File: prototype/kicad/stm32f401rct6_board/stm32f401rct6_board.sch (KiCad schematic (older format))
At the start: 1 part

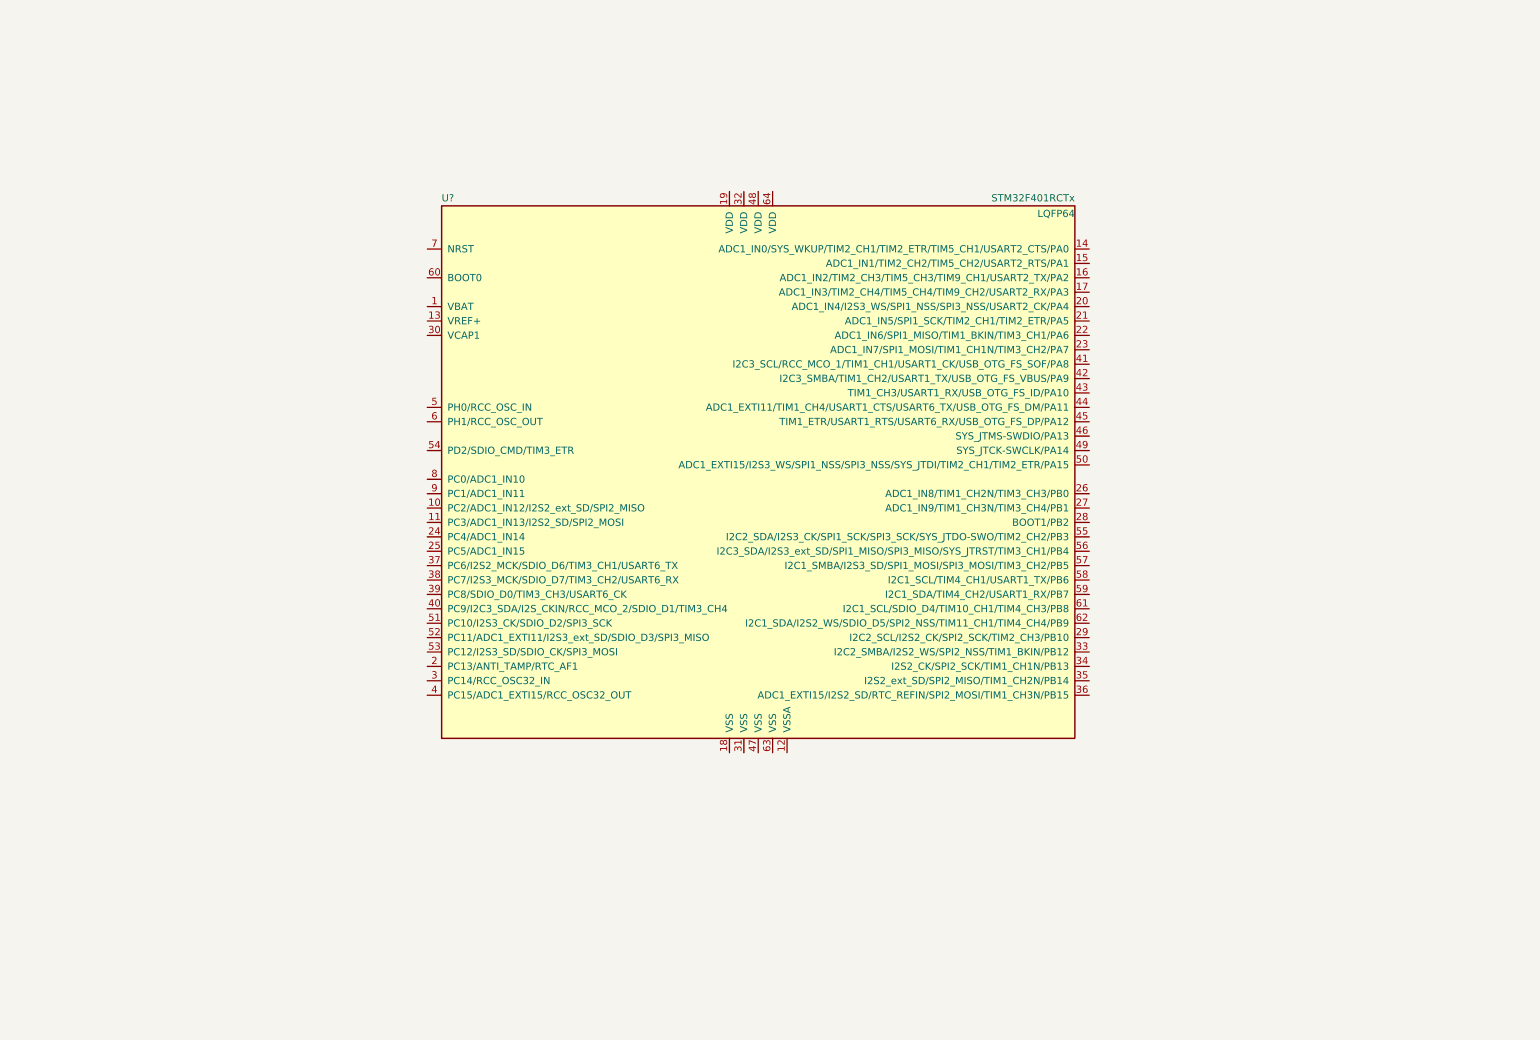
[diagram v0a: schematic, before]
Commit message: USART, boot switches, power supplies are implemented.
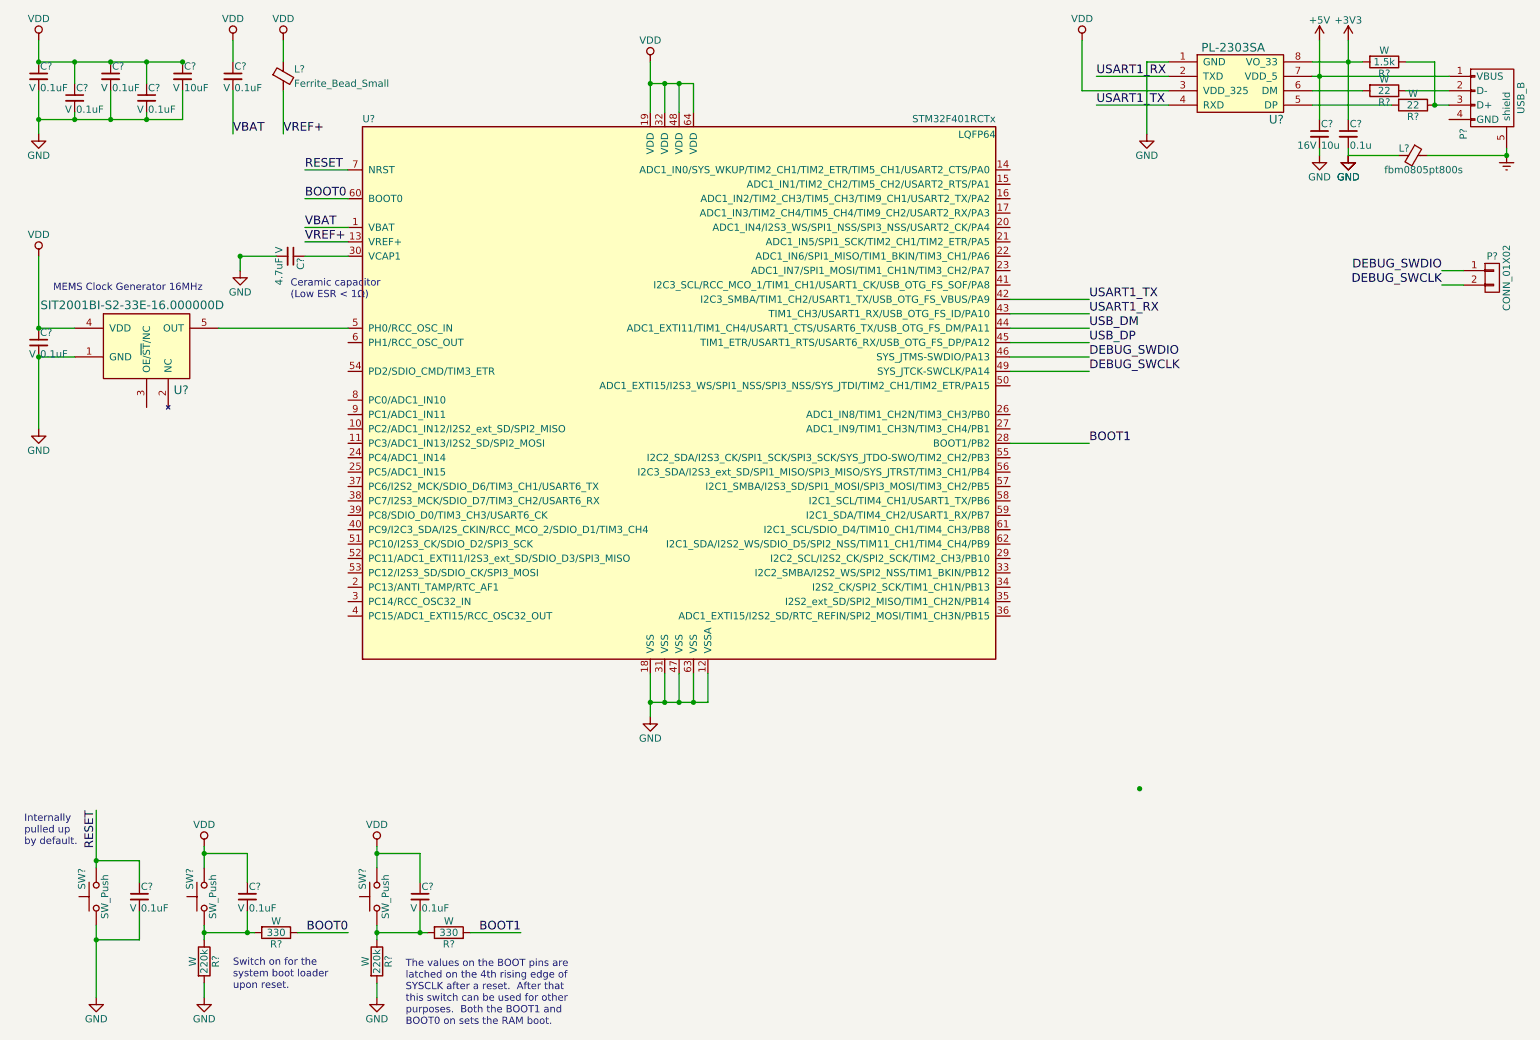
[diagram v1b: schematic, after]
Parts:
- added C? (x9): 0.1uF, symbol C_Small
- added C?: 10uF, symbol C_Small
- added C?: 4.7uF, symbol C_Small
- added C?: 10u, symbol C_Small
- added C?: 0.1u, symbol C_Small
- added L?: Ferrite_Bead_Small, symbol Ferrite_Bead_Small
- added L?: fbm0805pt800s, symbol Ferrite_Bead_Small
- added P?: CONN_01X02, symbol CONN_01X02
- added P?: USB_B, symbol USB_B
- added R? (x2): 220k, symbol R
- added R? (x2): 330, symbol R
- added R? (x2): 22, symbol R
- added R?: 1.5k, symbol R
- added SW? (x3): SW_Push, symbol SW_Push
- added U?: SIT2001BI-S2-33E-16.000000D, symbol SiT2001B
- added U?: PL-2303SA, symbol PL-2303SA
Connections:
- net VBAT: now reaches U?.1 (VBAT)
- net VBAT: now also C?.2
- net GND: now reaches U?.12 (VSSA)
- net GND: now also U?.18 (VSS), U?.31 (VSS), U?.47 (VSS), U?.63 (VSS), C?.2, C?.2, C?.2, C?.2, C?.2, C?.2, C?.2, C?.2, C?.2, C?.2, L?.2, R?.2, R?.2, SW?.1, U?.1 (GND), U?.1 (GND)
- net VREF+: now reaches U?.13 (VREF+)
- net VREF+: now also L?.2
- net VDD: now reaches U?.19 (VDD)
- net VDD: now also U?.32 (VDD), U?.48 (VDD), U?.64 (VDD), C?.1, C?.1, C?.1, C?.1, C?.1, C?.1, C?.1, C?.1, C?.1, L?.1, SW?.2, SW?.2, U?.3 (VDD_325), U?.4 (VDD)
- net BOOT1: now reaches U?.28 (BOOT1/PB2)
- net BOOT1: now also R?.1
- net at U?.30 (VCAP1): now also C?.1
- net USART1_TX: now reaches U?.42 (I2C3_SMBA/TIM1_CH2/USART1_TX/USB_OTG_FS_VBUS/PA9)
- net USART1_TX: now also U?.4 (RXD)
- net USART1_RX: now reaches U?.43 (TIM1_CH3/USART1_RX/USB_OTG_FS_ID/PA10)
- net USART1_RX: now also U?.2 (TXD)
- net USB_DM: now reaches U?.44 (ADC1_EXTI11/TIM1_CH4/USART1_CTS/USART6_TX/USB_OTG_FS_DM/PA11)
- net USB_DP: now reaches U?.45 (TIM1_ETR/USART1_RTS/USART6_RX/USB_OTG_FS_DP/PA12)
- net DEBUG_SWDIO: now reaches U?.46 (SYS_JTMS-SWDIO/PA13)
- net DEBUG_SWDIO: now also P?.1 (P1)
- net DEBUG_SWCLK: now reaches U?.49 (SYS_JTCK-SWCLK/PA14)
- net DEBUG_SWCLK: now also P?.2 (P2)
- net at U?.5 (PH0/RCC_OSC_IN): now also U?.5 (OUT)
- net BOOT0: now reaches U?.60 (BOOT0)
- net BOOT0: now also R?.1
- net RESET: now reaches U?.7 (NRST)
- net RESET: now also C?.1, SW?.2
- new net: C?.2, R?.1, R?.2, SW?.1 (x2)
- new net: R?.2, U?.5 (DP)
- new net: R?.2, U?.6 (DM)
- new net: P?.2 (D-), R?.1
- new net: P?.3 (D+), R?.1, R?.1
- new net +3V3: C?.1, R?.2, U?.8 (VO_33)
- new net +5V: C?.1, P?.1 (VBUS), U?.7 (VDD_5)
- new net Earth: L?.1, P?.5 (shield)
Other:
- note added: "Ceramic capacitor \n(Low ESR < 1Ω)"
- note added: "Internally\npulled up\nby default."
- note added: "MEMS Clock Generator 16MHz"
- note added: "Switch on for the\nsystem boot loader\nupon reset."
- note added: "The values on the BOOT pins are\nlatched on the 4th rising edge of\nSYSCLK after a reset. After that\nthis switch can be used for other\npurposes. Both the BOOT1 and\nBOOT0 on sets the RAM boot.\n"
- moved on the sheet: U?

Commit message: added some parts
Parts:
- added P?: USB_OTG, symbol USB_OTG
- added U?: STMPS2141STR, symbol STMPS2141STR
- added U?: EMIF02-USB03F2, symbol EMIF02-USB03F2
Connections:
- net GND: now also P?.4 (GND)
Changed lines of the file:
@@
 USB_DP
 $Comp
-L VDD #PWR?
+L VDD #PWR01
 U 1 1 592E7F1B
 P 750 2350
-F 0 "#PWR?" H 750 2200 50  0001 C CNN
+F 0 "#PWR01" H 750 2200 50  0001 C CNN
 F 1 "VDD" H 750 2500 50  0000 C CNN
 F 2 "" H 750 2350 50  0000 C CNN
@@
 $EndComp
 $Comp
-L GND #PWR?
+L GND #PWR02
 U 1 1 592E7F48
 P 750 3550
-F 0 "#PWR?" H 750 3300 50  0001 C CNN
+F 0 "#PWR02" H 750 3300 50  0001 C CNN
 F 1 "GND" H 750 3400 50  0000 C CNN
 F 2 "" H 750 3550 50  0000 C CNN
@@
 $EndComp
 $Comp
-L VDD #PWR?
+L VDD #PWR03
 U 1 1 592E82FC
 P 5000 1000
-F 0 "#PWR?" H 5000 850 50  0001 C CNN
+F 0 "#PWR03" H 5000 850 50  0001 C CNN
 F 1 "VDD" H 5000 1150 50  0000 C CNN
 F 2 "" H 5000 1000 50  0000 C CNN
@@
 $EndComp
 $Comp
-L GND #PWR?
+L GND #PWR04
 U 1 1 592E8A90
 P 750 1500
-F 0 "#PWR?" H 750 1250 50  0001 C CNN
+F 0 "#PWR04" H 750 1250 50  0001 C CNN
 F 1 "GND" H 750 1350 50  0000 C CNN
 F 2 "" H 750 1500 50  0000 C CNN
@@
 $EndComp
 $Comp
-L VDD #PWR?
+L VDD #PWR05
 U 1 1 592E8AD2
 P 750 850
-F 0 "#PWR?" H 750 700 50  0001 C CNN
+F 0 "#PWR05" H 750 700 50  0001 C CNN
 F 1 "VDD" H 750 1000 50  0000 C CNN
 F 2 "" H 750 850 50  0000 C CNN
@@
 $EndComp
 $Comp
-L VDD #PWR?
+L VDD #PWR06
 U 1 1 592E9827
 P 2100 850
-F 0 "#PWR?" H 2100 700 50  0001 C CNN
+F 0 "#PWR06" H 2100 700 50  0001 C CNN
 F 1 "VDD" H 2100 1000 50  0000 C CNN
 F 2 "" H 2100 850 50  0000 C CNN
@@
 VBAT
 $Comp
-L VDD #PWR?
+L VDD #PWR07
 U 1 1 592E99F2
 P 2450 850
-F 0 "#PWR?" H 2450 700 50  0001 C CNN
+F 0 "#PWR07" H 2450 700 50  0001 C CNN
 F 1 "VDD" H 2450 1000 50  0000 C CNN
 F 2 "" H 2450 850 50  0000 C CNN
@@
 $EndComp
 $Comp
-L GND #PWR?
+L GND #PWR08
 U 1 1 592EC658
 P 2150 2450
-F 0 "#PWR?" H 2150 2200 50  0001 C CNN
+F 0 "#PWR08" H 2150 2200 50  0001 C CNN
 F 1 "GND" H 2150 2300 50  0000 C CNN
 F 2 "" H 2150 2450 50  0000 C CNN
@@
 	7500 2950 8050 2950
 Wire Wire Line
-	5000 1000 5000 1150
-Wire Wire Line
-	5000 1150 5000 1350
+	5000 1000 5000 1350
 Wire Wire Line
 	5100 1350 5100 1150
@@
 	5300 1150 5300 1350
 Wire Wire Line
-	5000 1150 5100 1150
-Wire Wire Line
-	5100 1150 5200 1150
-Wire Wire Line
-	5200 1150 5300 1150
+	5000 1150 5300 1150
 Connection ~ 5000 1150
 Connection ~ 5200 1150
@@
 	750  850  750  1000
 Wire Wire Line
-	750  1000 1000 1000
-Wire Wire Line
-	1000 1000 1250 1000
-Wire Wire Line
-	1250 1000 1500 1000
-Wire Wire Line
-	1500 1000 1750 1000
-Wire Wire Line
-	750  1200 750  1400
-Wire Wire Line
-	750  1400 750  1500
+	750  1000 1750 1000
+Wire Wire Line
+	750  1200 750  1500
 Wire Wire Line
 	1000 1000 1000 1150
@@
 	1750 1400 1750 1200
 Wire Wire Line
-	750  1400 1000 1400
-Wire Wire Line
-	1000 1400 1250 1400
-Wire Wire Line
-	1250 1400 1500 1400
-Wire Wire Line
-	1500 1400 1750 1400
+	750  1400 1750 1400
 Connection ~ 1500 1400
 Connection ~ 1250 1400
@@
 	2150 2350 2150 2450
 Wire Wire Line
-	5000 5250 5000 5450
-Wire Wire Line
-	5000 5450 5000 5550
+	5000 5250 5000 5550
 Wire Wire Line
 	5100 5250 5100 5450
@@
 	5400 5450 5400 5250
 Wire Wire Line
-	5000 5450 5100 5450
-Wire Wire Line
-	5100 5450 5200 5450
-Wire Wire Line
-	5200 5450 5300 5450
-Wire Wire Line
-	5300 5450 5400 5450
+	5000 5450 5400 5450
 Connection ~ 5000 5450
 Connection ~ 5300 5450
@@
 Connection ~ 5100 5450
 $Comp
-L GND #PWR?
+L GND #PWR09
 U 1 1 592ED280
 P 5000 5550
-F 0 "#PWR?" H 5000 5300 50  0001 C CNN
+F 0 "#PWR09" H 5000 5300 50  0001 C CNN
 F 1 "GND" H 5000 5400 50  0000 C CNN
 F 2 "" H 5000 5550 50  0000 C CNN
@@
 RESET
 Wire Wire Line
-	1150 6200 1150 6550
-Wire Wire Line
-	1150 6550 1150 6600
+	1150 6200 1150 6600
 Text Label 1150 6200 3    60   ~ 0
 RESET
@@
 $EndComp
 Wire Wire Line
-	1150 7000 1150 7100
-Wire Wire Line
-	1150 7100 1150 7500
-$Comp
-L GND #PWR?
+	1150 7000 1150 7500
+$Comp
+L GND #PWR010
 U 1 1 592F0ABF
 P 1150 7500
-F 0 "#PWR?" H 1150 7250 50  0001 C CNN
+F 0 "#PWR010" H 1150 7250 50  0001 C CNN
 F 1 "GND" H 1150 7350 50  0000 C CNN
 F 2 "" H 1150 7500 50  0000 C CNN
@@
 	7500 3650 8050 3650
 Wire Wire Line
-	1900 6450 1900 6500
-Wire Wire Line
-	1900 6500 1900 6600
+	1900 6450 1900 6600
 $Comp
 L SW_Push SW?
@@
 	2200 6900 2200 7050
 Wire Wire Line
-	1900 7050 2200 7050
-Wire Wire Line
-	2200 7050 2250 7050
-Wire Wire Line
-	1900 7000 1900 7050
-Wire Wire Line
-	1900 7050 1900 7100
+	1900 7050 2250 7050
+Wire Wire Line
+	1900 7000 1900 7100
 $Comp
 L R R?
@@
 	1900 7400 1900 7500
 $Comp
-L GND #PWR?
+L GND #PWR011
 U 1 1 59301568
 P 1900 7500
-F 0 "#PWR?" H 1900 7250 50  0001 C CNN
+F 0 "#PWR011" H 1900 7250 50  0001 C CNN
 F 1 "GND" H 1900 7350 50  0000 C CNN
 F 2 "" H 1900 7500 50  0000 C CNN
@@
 BOOT0
 $Comp
-L VDD #PWR?
+L VDD #PWR012
 U 1 1 5930181B
 P 1900 6450
-F 0 "#PWR?" H 1900 6300 50  0001 C CNN
+F 0 "#PWR012" H 1900 6300 50  0001 C CNN
 F 1 "VDD" H 1900 6600 50  0000 C CNN
 F 2 "" H 1900 6450 50  0000 C CNN
@@
 Switch on for the\nsystem boot loader\nupon reset.
 Wire Wire Line
-	3100 6450 3100 6500
-Wire Wire Line
-	3100 6500 3100 6600
+	3100 6450 3100 6600
 $Comp
 L SW_Push SW?
@@
 	3400 6900 3400 7050
 Wire Wire Line
-	3100 7050 3400 7050
-Wire Wire Line
-	3400 7050 3450 7050
-Wire Wire Line
-	3100 7000 3100 7050
-Wire Wire Line
-	3100 7050 3100 7100
+	3100 7050 3450 7050
+Wire Wire Line
+	3100 7000 3100 7100
 $Comp
 L R R?
@@
 	3100 7400 3100 7500
 $Comp
-L GND #PWR?
+L GND #PWR013
 U 1 1 59305A95
 P 3100 7500
-F 0 "#PWR?" H 3100 7250 50  0001 C CNN
+F 0 "#PWR013" H 3100 7250 50  0001 C CNN
 F 1 "GND" H 3100 7350 50  0000 C CNN
 F 2 "" H 3100 7500 50  0000 C CNN
@@
 BOOT1
 $Comp
-L VDD #PWR?
+L VDD #PWR014
 U 1 1 59305A9C
 P 3100 6450
-F 0 "#PWR?" H 3100 6300 50  0001 C CNN
+F 0 "#PWR014" H 3100 6300 50  0001 C CNN
 F 1 "VDD" H 3100 6600 50  0000 C CNN
 F 2 "" H 3100 6450 50  0000 C CNN
@@
 	10450 1300 10550 1300
 Wire Wire Line
-	9600 1000 9850 1000
-Wire Wire Line
-	9850 1000 9950 1000
-Wire Wire Line
-	9850 850  9850 1000
-Wire Wire Line
-	9850 1000 9850 1400
-$Comp
-L +3V3 #PWR?
+	9600 1000 9950 1000
+Wire Wire Line
+	9850 850  9850 1400
+$Comp
+L +3V3 #PWR015
 U 1 1 5930BAD8
 P 9850 850
-F 0 "#PWR?" H 9850 700 50  0001 C CNN
+F 0 "#PWR015" H 9850 700 50  0001 C CNN
 F 1 "+3V3" H 9850 990 50  0000 C CNN
 F 2 "" H 9850 850 50  0000 C CNN
@@
 Connection ~ 10450 1300
 Wire Wire Line
-	9600 1100 9650 1100
-Wire Wire Line
-	9650 1100 10550 1100
-Wire Wire Line
-	9650 850  9650 1100
-Wire Wire Line
-	9650 1100 9650 1400
-$Comp
-L +5V #PWR?
+	9600 1100 10550 1100
+Wire Wire Line
+	9650 850  9650 1400
+$Comp
+L +5V #PWR016
 U 1 1 5930BEBB
 P 9650 850
-F 0 "#PWR?" H 9650 700 50  0001 C CNN
+F 0 "#PWR016" H 9650 700 50  0001 C CNN
 F 1 "+5V" H 9650 990 50  0000 C CNN
 F 2 "" H 9650 850 50  0000 C CNN
@@
 	8600 1200 8000 1200
 $Comp
-L VDD #PWR?
+L VDD #PWR017
 U 1 1 5930D59E
 P 8000 850
-F 0 "#PWR?" H 8000 700 50  0001 C CNN
+F 0 "#PWR017" H 8000 700 50  0001 C CNN
 F 1 "VDD" H 8000 1000 50  0000 C CNN
 F 2 "" H 8000 850 50  0000 C CNN
@@
 	9650 1600 9650 1650
 $Comp
-L GND #PWR?
+L GND #PWR018
 U 1 1 5930DE58
 P 9650 1650
-F 0 "#PWR?" H 9650 1400 50  0001 C CNN
+F 0 "#PWR018" H 9650 1400 50  0001 C CNN
 F 1 "GND" H 9650 1500 50  0000 C CNN
 F 2 "" H 9650 1650 50  0000 C CNN
@@
 $EndComp
 $Comp
-L GND #PWR?
+L GND #PWR019
 U 1 1 5930DEBA
 P 9850 1650
-F 0 "#PWR?" H 9850 1400 50  0001 C CNN
+F 0 "#PWR019" H 9850 1400 50  0001 C CNN
 F 1 "GND" H 9850 1500 50  0000 C CNN
 F 2 "" H 9850 1650 50  0000 C CNN
@@
 	8450 1000 8450 1500
 $Comp
-L GND #PWR?
+L GND #PWR020
 U 1 1 5930EAF1
 P 8450 1500
-F 0 "#PWR?" H 8450 1250 50  0001 C CNN
+F 0 "#PWR020" H 8450 1250 50  0001 C CNN
 F 1 "GND" H 8450 1350 50  0000 C CNN
 F 2 "" H 8450 1500 50  0000 C CNN
@@
 	10950 1600 10950 1650
 $Comp
-L Earth #PWR?
+L Earth #PWR021
 U 1 1 593101D8
 P 10950 1650
-F 0 "#PWR?" H 10950 1400 50  0001 C CNN
+F 0 "#PWR021" H 10950 1400 50  0001 C CNN
 F 1 "Earth" H 10950 1500 50  0001 C CNN
 F 2 "" H 10950 1650 50  0000 C CNN
@@
 $EndComp
 $Comp
-L GND #PWR?
+L GND #PWR022
 U 1 1 59310520
 P 9850 1650
-F 0 "#PWR?" H 9850 1400 50  0001 C CNN
+F 0 "#PWR022" H 9850 1400 50  0001 C CNN
 F 1 "GND" H 9850 1500 50  0000 C CNN
 F 2 "" H 9850 1650 50  0000 C CNN
@@
 Text Notes 850  2600 0    50   ~ 0
 MEMS Clock Generator 16MHz
-Connection ~ 8400 6050
+$Comp
+L USB_OTG P?
+U 1 1 59311065
+P 10850 4250
+F 0 "P?" H 11175 4125 50  0000 C CNN
+F 1 "USB_OTG" H 10850 4450 50  0000 C CNN
+F 2 "" V 10800 4150 50  0000 C CNN
+F 3 "" V 10800 4150 50  0000 C CNN
+	1    10850 4250
+	0    1    1    0
+$EndComp
+$Comp
+L GND #PWR023
+U 1 1 59311523
+P 10500 1400
+F 0 "#PWR023" H 10500 1150 50  0001 C CNN
+F 1 "GND" H 10500 1250 50  0000 C CNN
+F 2 "" H 10500 1400 50  0000 C CNN
+F 3 "" H 10500 1400 50  0000 C CNN
+	1    10500 1400
+	1    0    0    -1
+$EndComp
+Wire Wire Line
+	10550 1400 10500 1400
+$Comp
+L STMPS2141STR U?
+U 1 1 593128F4
+P 9050 4000
+F 0 "U?" H 8850 4225 60  0000 C CNN
+F 1 "STMPS2141STR" H 9125 3800 60  0000 C CNN
+F 2 "" H 9025 3175 60  0001 C CNN
+F 3 "" H 9025 3175 60  0001 C CNN
+	1    9050 4000
+	1    0    0    -1
+$EndComp
+$Comp
+L EMIF02-USB03F2 U?
+U 1 1 59312985
+P 9250 5150
+F 0 "U?" H 9025 5500 60  0000 C CNN
+F 1 "EMIF02-USB03F2" H 9350 4800 60  0000 C CNN
+F 2 "" H 9075 5200 60  0001 C CNN
+F 3 "" H 9075 5200 60  0001 C CNN
+	1    9250 5150
+	1    0    0    -1
+$EndComp
 $EndSCHEMATC
